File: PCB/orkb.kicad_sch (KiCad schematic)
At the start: 1 part, among them U1 ProMicro

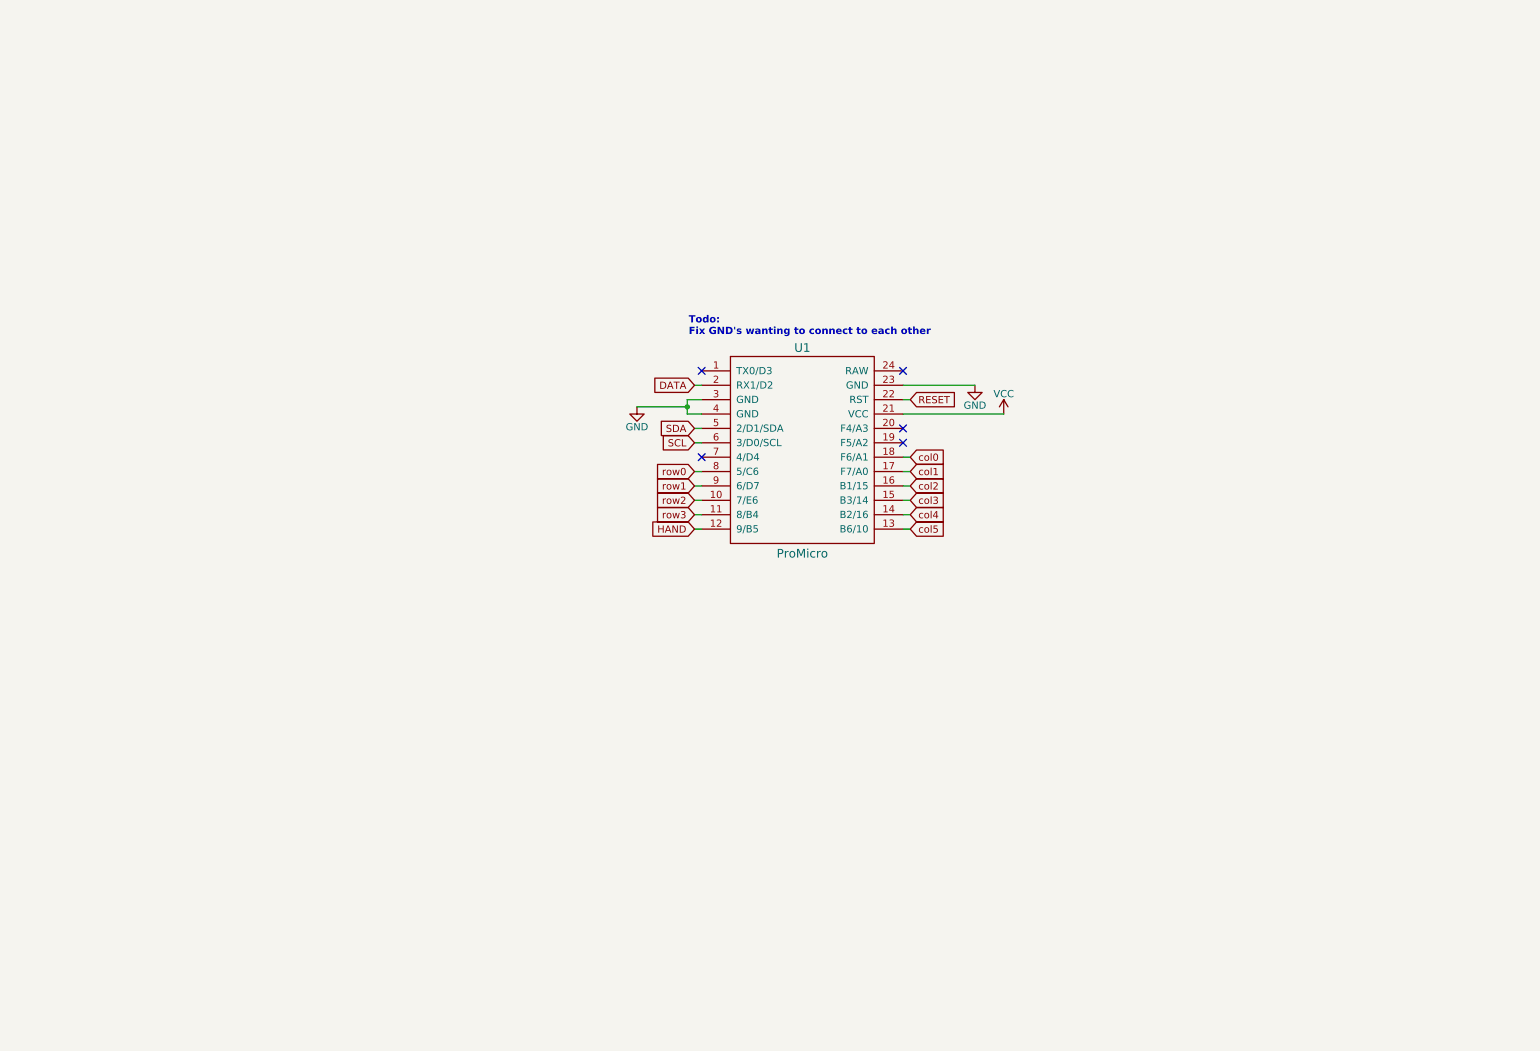
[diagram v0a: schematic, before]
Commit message: Draft schematic components
[Pending]
Import to PCB
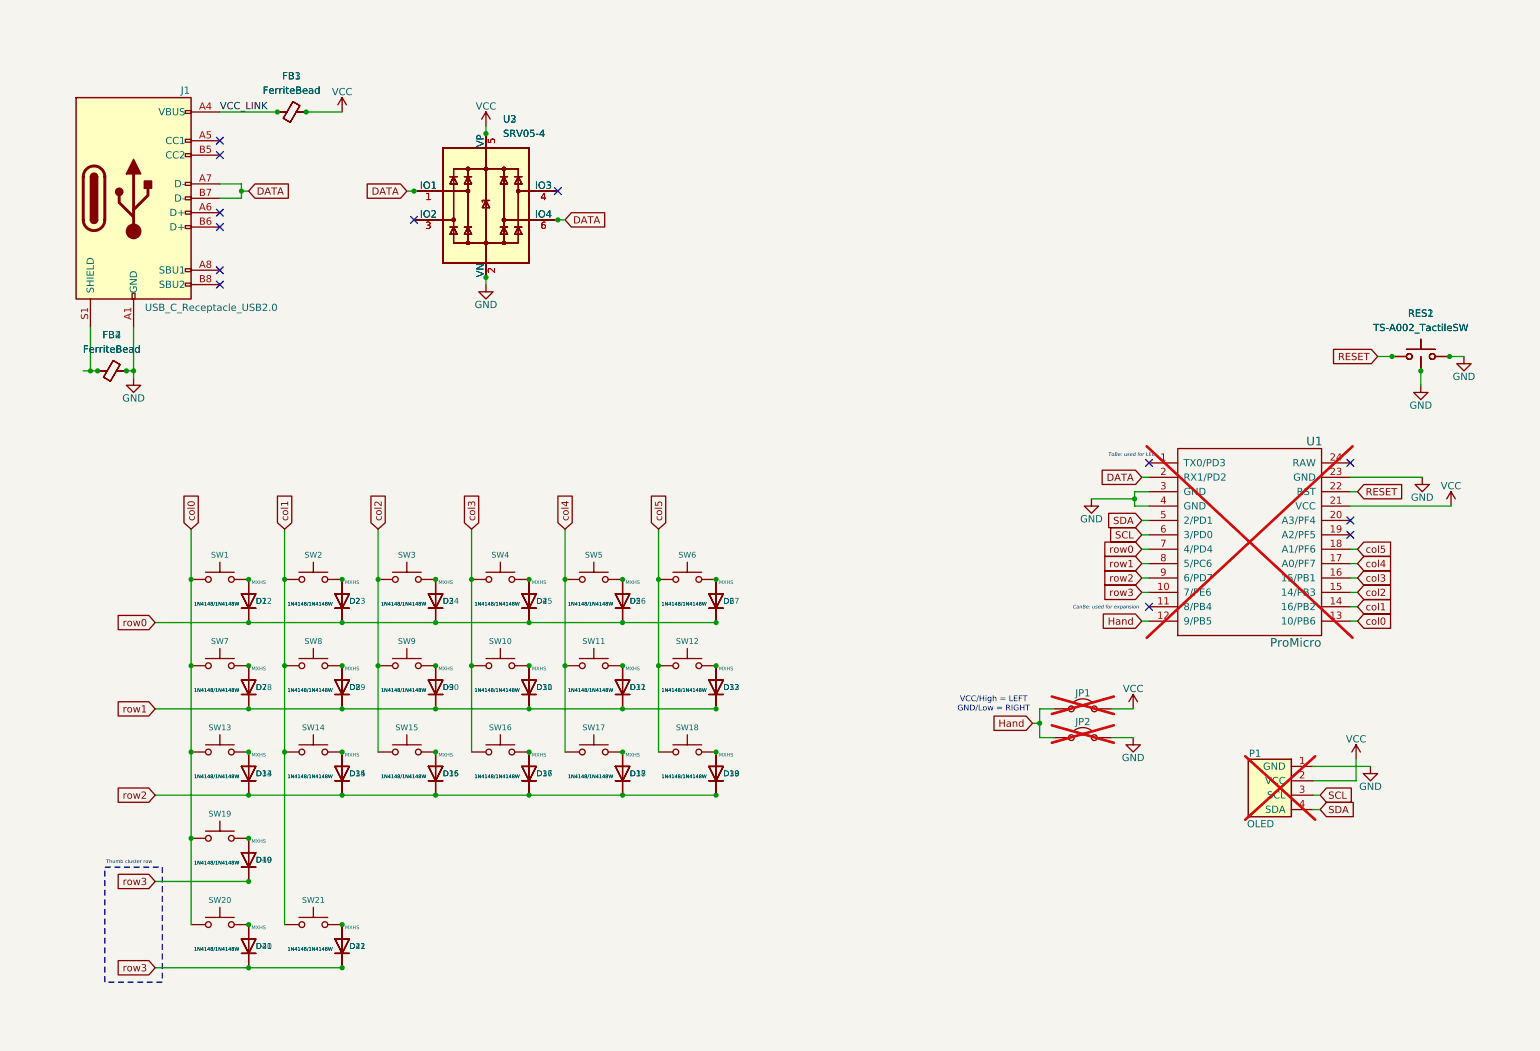
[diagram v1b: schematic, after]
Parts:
- removed U1: ProMicro, keyboard_reversible:ProMicro_unrouted, symbol kbd:ProMicro
- added D1, D10, D11, D12, D13, D14, D15, D16, D17, D18, D19, D2, D20, D21, D22, D23, D24, D25, D26, D27, D28, D29, D3, D30, D31, D32, D33, D34, D35, D36, D37, D38, D39, D4, D40, D41, D42, D5, D6, D7, D8, D9: 1N4148/1N4148W, symbol Device:D
- added FB1, FB2, FB3, FB4: FerriteBead, symbol Device:FerriteBead_Small
- added J1: USB_C_Receptacle_USB2.0, Keyboard Common:Molex-216990_GCT-USB45xx_HRO-TYPE-C-31-M-13x-PiMicro_1_DOUBLESIDED, symbol SplitKeyboard_Common:USB_C_Receptacle_USB2.0
- added JP1, JP2: Jumper_2, symbol Jumper:Jumper_2_Open
- added P1: OLED, Keyboard Common:SSD1306-0.91-OLED-4pin-128x32 doublesided, symbol SplitKeyboard_Common:OLED_4pin
- added RES1, RES2: TS-A002_TactileSW, Keyboard Common:YTS-A002, symbol SplitKeyboard_Common:TS-A002_TactileSW
- added SW1, SW10, SW11, SW12, SW13, SW14, SW15, SW16, SW17, SW18, SW19, SW2, SW20, SW21, SW3, SW4, SW5, SW6, SW7, SW8, SW9: MXHS, symbol Switch:SW_Push
- added U1: ProMicro, Keyboard Controllers:ProMicro_jumpers_V2, symbol SplitKeyboard_Common:ProMicro_Jumpers_v2
- added U2, U3: SRV05-4, Package_TO_SOT_SMD:SOT-23-6, symbol Power_Protection:SRV05-4
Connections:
- net DATA: now also J1.A7 (D-), J1.B7 (D-), U1.2 (RX1/PD2), U2.1 (IO1), U2.6 (IO4), U3.1 (IO1), U3.6 (IO4)
- net GND: now also FB2.2, FB4.2, J1.A1 (GND), J1.A12 (GND), J1.B1 (GND), J1.B12 (GND), JP2.2 (B), P1.1 (GND), RES1.2, RES1.3, RES2.2, RES2.3, U1.23 (GND), U1.3 (GND), U1.4 (GND), U2.2 (VN), U3.2 (VN)
- net RESET: now also RES1.1, RES2.1, U1.22 (RST)
- net SCL: now also P1.3 (SCL), U1.6 (3/PD0)
- net SDA: now also P1.4 (SDA), U1.5 (2/PD1)
- net VCC: now also FB1.2, FB3.2, JP1.2 (B), P1.2 (VCC), U1.21 (VCC), U2.5 (VP), U3.5 (VP)
- net col0: now also SW1.1, SW13.1, SW19.1, SW20.1, SW7.1, U1.13 (10/PB6)
- net col1: now also SW14.1, SW2.1, SW21.1, SW8.1, U1.14 (16/PB2)
- net col2: now also SW15.1, SW3.1, SW9.1, U1.15 (14/PB3)
- net col3: now also SW10.1, SW16.1, SW4.1, U1.16 (15/PB1)
- net col4: now also SW11.1, SW17.1, SW5.1, U1.17 (A0/PF7)
- net col5: now also SW12.1, SW18.1, SW6.1, U1.18 (A1/PF6)
- net row0: now also D1.1 (K), D2.1 (K), D22.1 (K), D23.1 (K), D24.1 (K), D25.1 (K), D26.1 (K), D27.1 (K), D3.1 (K), D4.1 (K), D5.1 (K), D6.1 (K), U1.7 (4/PD4)
- net row1: now also D10.1 (K), D11.1 (K), D12.1 (K), D28.1 (K), D29.1 (K), D30.1 (K), D31.1 (K), D32.1 (K), D33.1 (K), D7.1 (K), D8.1 (K), D9.1 (K), U1.8 (5/PC6)
- net row2: now also D13.1 (K), D14.1 (K), D15.1 (K), D16.1 (K), D17.1 (K), D18.1 (K), D34.1 (K), D35.1 (K), D36.1 (K), D37.1 (K), D38.1 (K), D39.1 (K), U1.9 (6/PD7)
- net row3: now also D19.1 (K), D20.1 (K), D21.1 (K), D40.1 (K), D41.1 (K), D42.1 (K), U1.10 (7/PE6)
- new net: D1.2 (A), D22.2 (A), SW1.2
- new net: U2.3 (IO2), U3.3 (IO2)
- new net: U2.4 (IO3), U3.4 (IO3)
- new net: D19.2 (A), D40.2 (A), SW19.2
- new net: D18.2 (A), D39.2 (A), SW18.2
- new net: D14.2 (A), D35.2 (A), SW14.2
- new net: D2.2 (A), D23.2 (A), SW2.2
- new net: D17.2 (A), D38.2 (A), SW17.2
- new net: FB2.1, FB4.1, J1.S1 (SHIELD)
- new net: D13.2 (A), D34.2 (A), SW13.2
- new net: U1.A (0), U1.B (0), U1.C (0), U1.D (0), U1.E (0), U1.F (0), U1.G (0), U1.H (0), U1.I (0), U1.J (0), U1.K (0), U1.L (0), U1.M (0), U1.N (0), U1.O (0), U1.P (0), U1.Q (0), U1.R (0), U1.S (0), U1.T (0), U1.U (0), U1.V (0), U1.X (0), U1.Y (0)
- new net: D28.2 (A), D7.2 (A), SW7.2
- new net: D12.2 (A), D33.2 (A), SW12.2
- new net: D15.2 (A), D36.2 (A), SW15.2
- new net: D25.2 (A), D4.2 (A), SW4.2
- new net: D16.2 (A), D37.2 (A), SW16.2
- new net: D11.2 (A), D32.2 (A), SW11.2
- new net: D20.2 (A), D41.2 (A), SW20.2
- new net: D10.2 (A), D31.2 (A), SW10.2
- new net: D21.2 (A), D42.2 (A), SW21.2
- new net: D27.2 (A), D6.2 (A), SW6.2
- new net: D26.2 (A), D5.2 (A), SW5.2
- new net: D30.2 (A), D9.2 (A), SW9.2
- new net: D29.2 (A), D8.2 (A), SW8.2
- new net: D24.2 (A), D3.2 (A), SW3.2
- new net: P1.A (0), P1.B (0), P1.C (0), P1.D (0)
- new net Hand: JP1.1 (A), JP2.1 (A), U1.12 (9/PB5)
- new net VCC_LINK: FB1.1, FB3.1, J1.A4 (VBUS), J1.A9 (VBUS), J1.B4 (VBUS), J1.B9 (VBUS)
- no-connect marks 5 -> 13
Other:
- note added: "CanBe: used for expansion"
- note added: "Thumb cluster row"
- note added: "ToBe: used for LED"
- note added: "VCC/High = LEFT GND/Low = RIGHT"
- note removed: "Todo: Fix GND's wanting to connect to each other"

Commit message: Keyboard layout and switch positioning
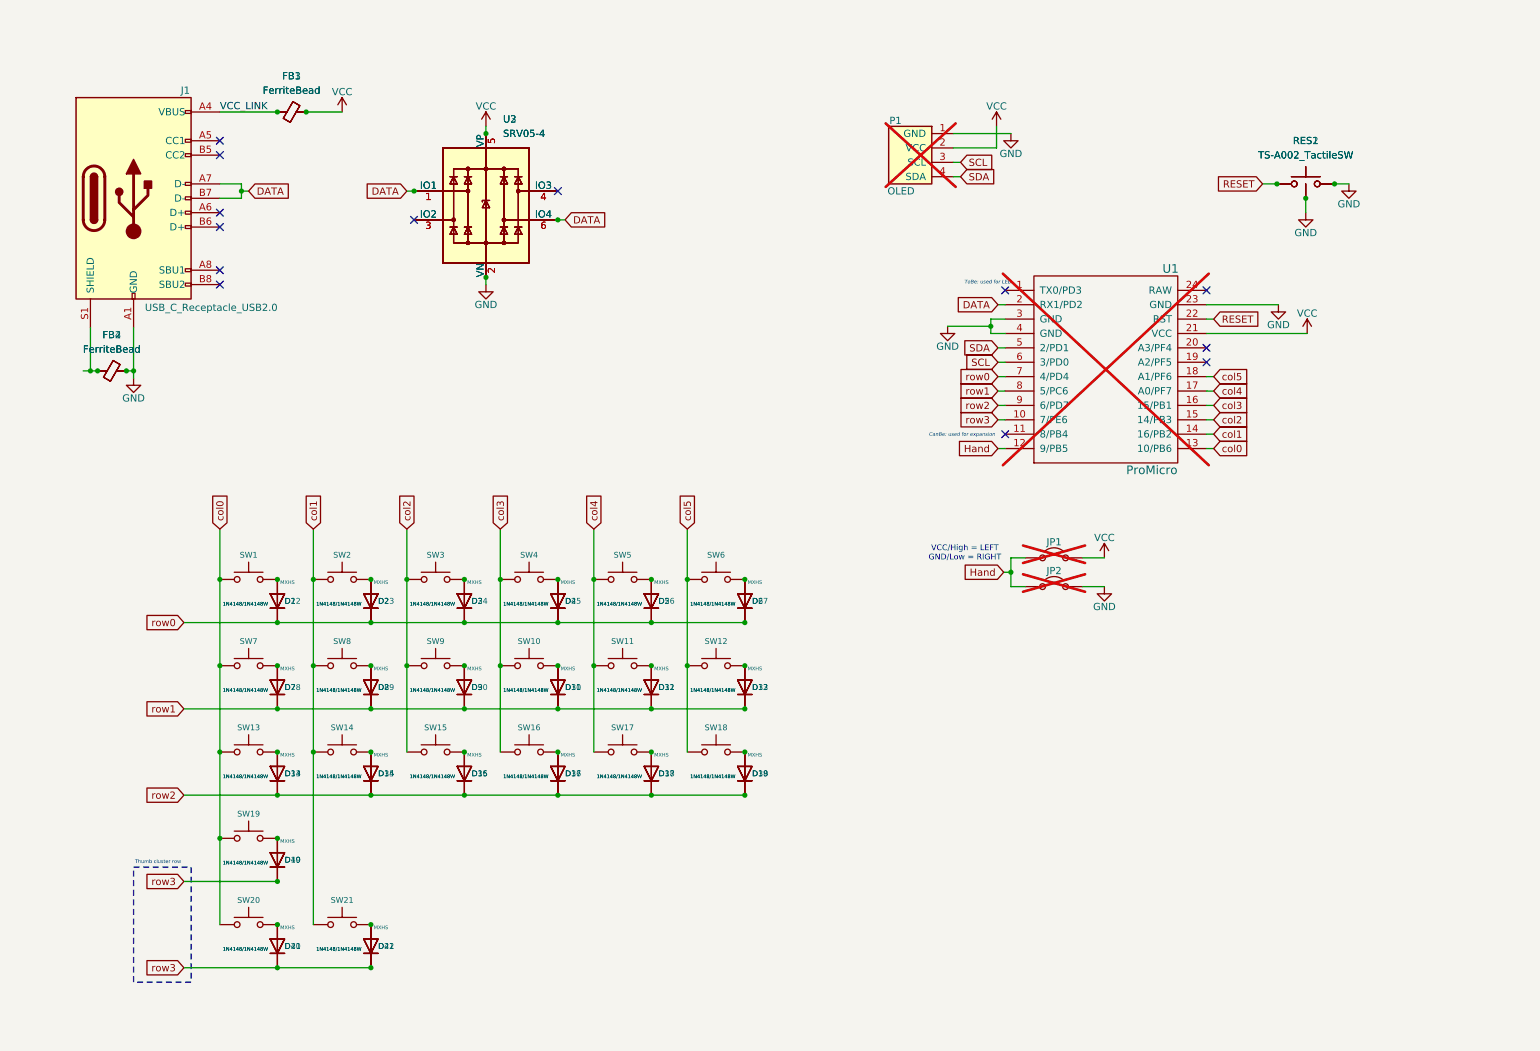
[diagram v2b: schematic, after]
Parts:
- D1, D10, D11, D12, D13, D14, D15, D16, D17, D18, D19, D2, D20, D21, D22, D23, D24, D25, D26, D27, D28, D29, D3, D30, D31, D32, D33, D34, D35, D36, D37, D38, D39, D4, D40, D41, D42, D5, D6, D7, D8, D9: footprint (none) -> SplitKeyboard_Common:Diode_DO35_SOD123_Hybrid
- FB1, FB2, FB3, FB4: footprint (none) -> Capacitor_SMD:C_0603_1608Metric_Pad1.08x0.95mm_HandSolder
- J1: footprint Keyboard Common:Molex-216990_GCT-USB45xx_HRO-TYPE-C-31-M-13x-PiMicro_1_DOUBLESIDED -> SplitKeyboard_Common:HRO-TYPE-C-31-M-13x_DOUBLESIDED_Molex-216990_GCT-USB45xx
- JP1, JP2: footprint (none) -> Jumper:SolderJumper-2_P1.3mm_Open_TrianglePad1.0x1.5mm
- P1: footprint Keyboard Common:SSD1306-0.91-OLED-4pin-128x32 doublesided -> SplitKeyboard_Common:SSD1306-0.91-OLED-4pin-128x32_DOUBLESIDED
- RES1, RES2: footprint Keyboard Common:YTS-A002 -> SplitKeyboard_Common:YTS-A002
- SW1, SW10, SW11, SW12, SW13, SW14, SW15, SW16, SW17, SW18, SW19, SW2, SW20, SW21, SW3, SW4, SW5, SW6, SW7, SW8, SW9: footprint (none) -> SplitKeyboard_Common:SW_MX_HotSwap_Reversible
- U1: footprint Keyboard Controllers:ProMicro_jumpers_V2 -> SplitKeyboard_Common:ProMicro_Jumpers_V2
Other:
- moved on the sheet: D1, D10, D11, D12, D13, D14, D15, D16, D17, D18, D19, D2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

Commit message: Refactoring entire project
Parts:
- added D43, D44: 1N4841/1N4148W, SplitKeyboard_Common:Diode_DO35_SOD123_Hybrid, symbol Device:D
- added SW22: MXHS, SplitKeyboard_Common:SW_MX_HotSwap_Reversible, symbol Switch:SW_Push
- D1, D10, D11, D12, D13, D14, D15, D16, D17, D18, D19, D2, D20, D21, D22, D23, D24, D25, D26, D27, D28, D29, D3, D30, D31, D32, D33, D34, D35, D36, D37, D38, D39, D4, D40, D41, D42, D5, D6, D7, D8, D9: value 1N4148/1N4148W -> 1N4841/1N4148W
- JP1, JP2: value Jumper_2 -> Jumper_2_Open; footprint Jumper:SolderJumper-2_P1.3mm_Open_TrianglePad1.0x1.5mm -> SplitKeyboard_Common:Jumper_min_v2; now fitted
- P1, U1: now fitted
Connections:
- net col0: no longer SW20.1
- net col1: now also SW20.1; no longer SW21.1
- net col2: now also SW21.1
- net col3: now also SW22.1
- net row0: now also D28.1 (K); no longer D22.1 (K)
- net row1: now also D34.1 (K); no longer D28.1 (K)
- net row2: now also D40.1 (K); no longer D34.1 (K)
- net row3: now also D22.1 (K), D43.1 (K), D44.1 (K); no longer D40.1 (K)
- net at D1.2 (A), SW1.2: now also D23.2 (A); no longer D22.2 (A)
- net at D19.2 (A), SW19.2: now also D41.2 (A); no longer D40.2 (A)
- net at D18.2 (A), SW18.2: now also D40.2 (A); no longer D39.2 (A)
- net at D14.2 (A), SW14.2: now also D36.2 (A); no longer D35.2 (A)
- net at D2.2 (A), SW2.2: now also D24.2 (A); no longer D23.2 (A)
- net at D17.2 (A), SW17.2: now also D39.2 (A); no longer D38.2 (A)
- net at D13.2 (A), SW13.2: now also D35.2 (A); no longer D34.2 (A)
- net at D7.2 (A), SW7.2: now also D29.2 (A); no longer D28.2 (A)
- net at D12.2 (A), SW12.2: now also D34.2 (A); no longer D33.2 (A)
- net at D15.2 (A), SW15.2: now also D37.2 (A); no longer D36.2 (A)
- net at D4.2 (A), SW4.2: now also D26.2 (A); no longer D25.2 (A)
- net at D16.2 (A), SW16.2: now also D38.2 (A); no longer D37.2 (A)
- net at D11.2 (A), SW11.2: now also D33.2 (A); no longer D32.2 (A)
- net at D20.2 (A), SW20.2: now also D42.2 (A); no longer D41.2 (A)
- net at D10.2 (A), SW10.2: now also D32.2 (A); no longer D31.2 (A)
- net at D21.2 (A), SW21.2: now also D43.2 (A); no longer D42.2 (A)
- net at D6.2 (A), SW6.2: now also D28.2 (A); no longer D27.2 (A)
- net at D5.2 (A), SW5.2: now also D27.2 (A); no longer D26.2 (A)
- net at D9.2 (A), SW9.2: now also D31.2 (A); no longer D30.2 (A)
- net at D8.2 (A), SW8.2: now also D30.2 (A); no longer D29.2 (A)
- net at D3.2 (A), SW3.2: now also D25.2 (A); no longer D24.2 (A)
- new net: D22.2 (A), D44.2 (A), SW22.2
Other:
- note added: "Thumb cluster"
- note added: "VCC = LEFT GND = RIGHT"
- note removed: "CanBe: used for expansion"
- note removed: "Thumb cluster row"
- note removed: "VCC/High = LEFT GND/Low = RIGHT"

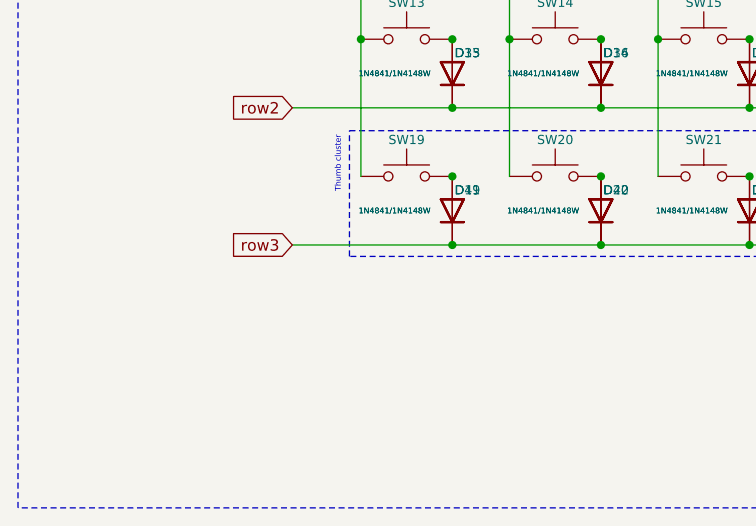
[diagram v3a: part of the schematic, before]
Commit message: Added extra index finger switch
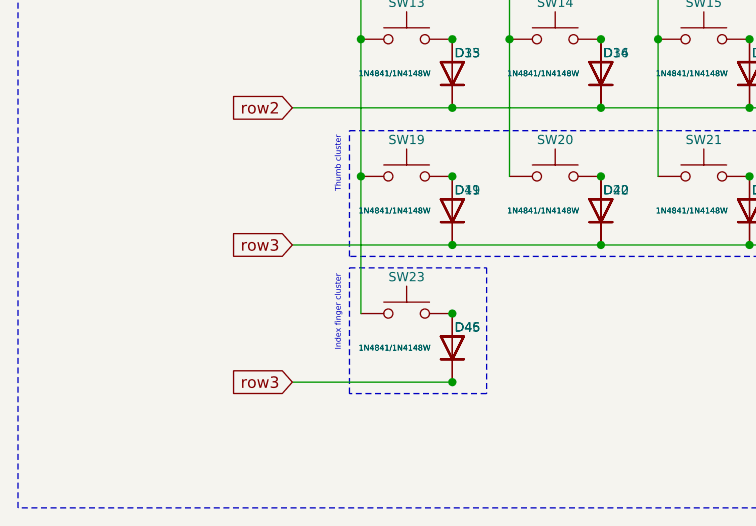
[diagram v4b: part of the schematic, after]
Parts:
- added D45, D46: 1N4841/1N4148W, SplitKeyboard_Common:Diode_DO35_SOD123_Hybrid, symbol Device:D
- added SW23: MXHS, SplitKeyboard_Common:SW_MX_HotSwap_Reversible, symbol Switch:SW_Push
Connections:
- net col0: now also SW23.1
- net row3: now also D45.1 (K), D46.1 (K)
- new net: D45.2 (A), D46.2 (A), SW23.2
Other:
- note added: "Index finger cluster"
